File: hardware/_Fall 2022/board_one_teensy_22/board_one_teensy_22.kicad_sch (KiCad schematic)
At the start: 12 parts, among them J1 Conn_01x04, U1 Teensy4.1, U2 BNO055_Breakout, U3 MPL3115A2_Breakout

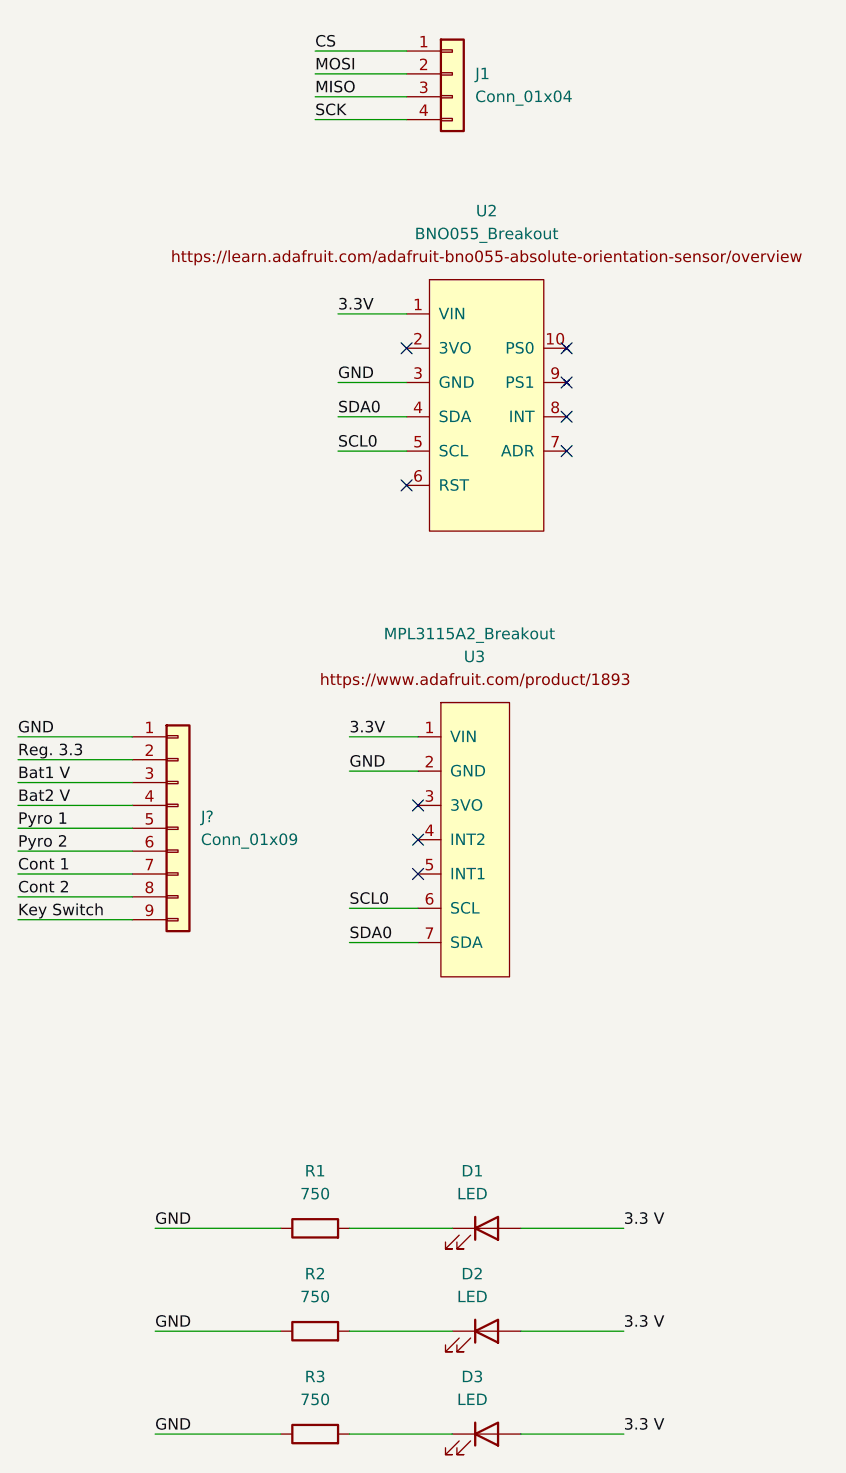
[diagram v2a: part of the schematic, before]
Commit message: Change minor labeling error in teensy boards kicad
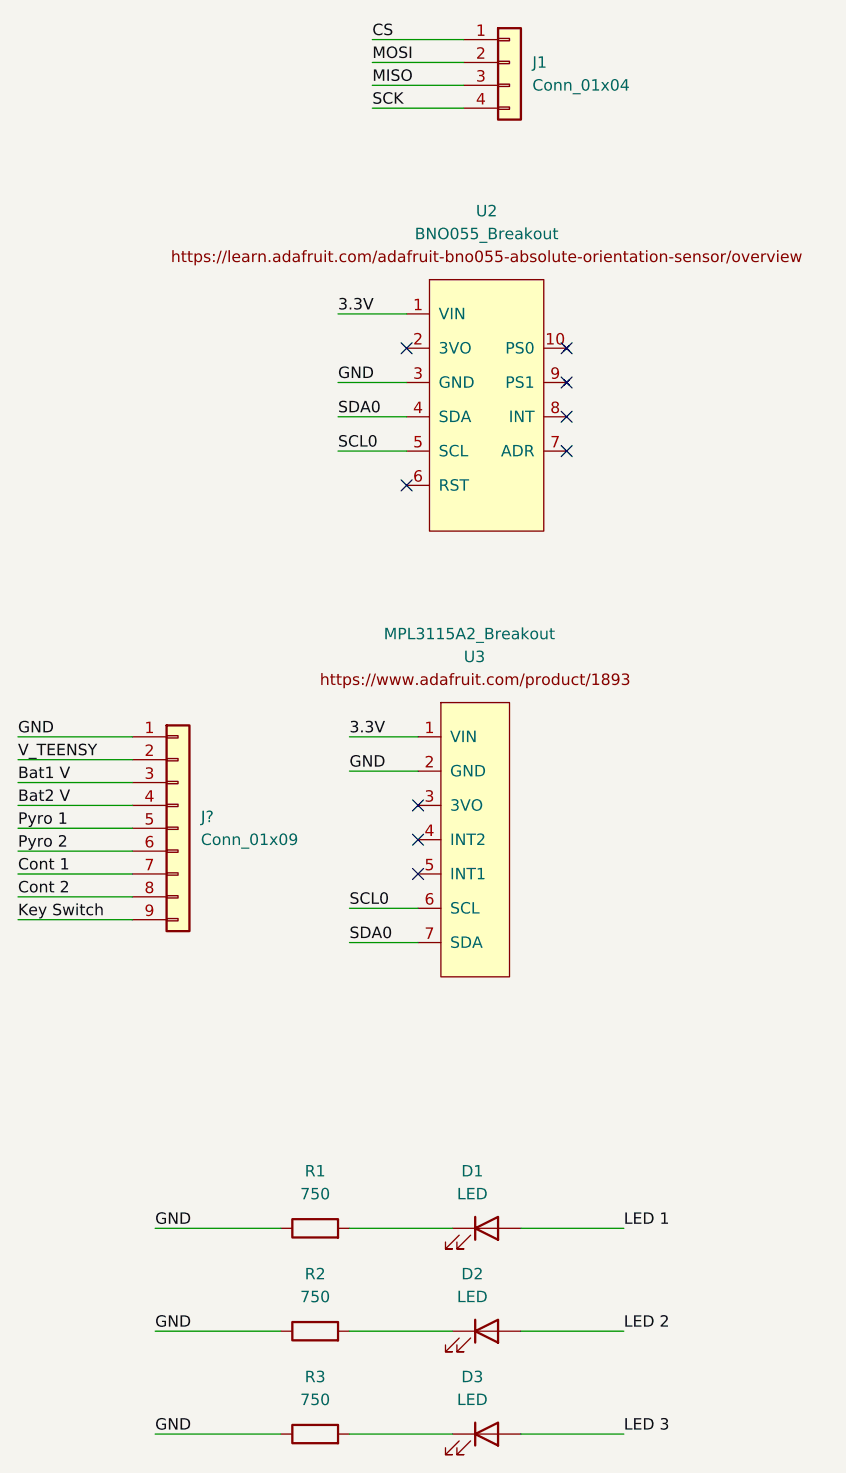
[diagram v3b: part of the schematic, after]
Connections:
- net Reg. 3.3 is gone; now on net V_TEENSY: J?.2 (Pin_2)
- net LED 1: now also D1.2 (A)
- net LED 2: now also D2.2 (A)
- net LED 3: now also D3.2 (A)
- removed net 3.3 V: D1.2 (A), D2.2 (A), D3.2 (A)
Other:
- moved on the sheet: J1
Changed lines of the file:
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@@
   (no_connect (at 95.25 74.93))
   (no_connect (at 231.14 48.26))
-  (wire (pts (xy 85.09 26.67) (xy 95.25 26.67))
+  (wire (pts (xy 91.44 25.4) (xy 101.6 25.4))
     (stroke (width 0) (type default) (color 0 0 0 0))
   )
@@
     (stroke (width 0) (type default) (color 0 0 0 0))
   )
-  (wire (pts (xy 85.09 31.75) (xy 95.25 31.75))
+  (wire (pts (xy 91.44 30.48) (xy 101.6 30.48))
     (stroke (width 0) (type default) (color 0 0 0 0))
   )
@@
     (stroke (width 0) (type default) (color 0 0 0 0))
   )
-  (wire (pts (xy 85.09 29.21) (xy 95.25 29.21))
+  (wire (pts (xy 91.44 27.94) (xy 101.6 27.94))
     (stroke (width 0) (type default) (color 0 0 0 0))
   )
@@
     (stroke (width 0) (type default) (color 0 0 0 0))
   )
-  (wire (pts (xy 85.09 34.29) (xy 95.25 34.29))
+  (wire (pts (xy 91.44 33.02) (xy 101.6 33.02))
     (stroke (width 0) (type default) (color 0 0 0 0))
   )
@@
     (stroke (width 0) (type default) (color 0 0 0 0))
   )
+  (label "LED 1" (at 119.38 157.48 0)
+    (effects (font (size 1.27 1.27)) (justify left bottom))
+  )
   (label "3.3V" (at 87.63 55.88 0)
     (effects (font (size 1.27 1.27)) (justify left bottom))
   )
-  (label "MISO" (at 85.09 31.75 0)
+  (label "MISO" (at 91.44 30.48 0)
     (effects (font (size 1.27 1.27)) (justify left bottom))
   )
@@
     (effects (font (size 1.27 1.27)) (justify left bottom))
   )
+  (label "LED 2" (at 119.38 168.91 0)
+    (effects (font (size 1.27 1.27)) (justify left bottom))
+  )
   (label "Pyro 2" (at 52.07 115.57 0)
     (effects (font (size 1.27 1.27)) (justify left bottom))
@@
     (effects (font (size 1.27 1.27)) (justify left bottom))
   )
-  (label "Reg. 3.3" (at 52.07 105.41 0)
+  (label "V_TEENSY" (at 52.07 105.41 0)
     (effects (font (size 1.27 1.27)) (justify left bottom))
   )
@@
     (effects (font (size 1.27 1.27)) (justify left bottom))
   )
-  (label "3.3 V" (at 119.38 157.48 0)
-    (effects (font (size 1.27 1.27)) (justify left bottom))
-  )
   (label "Key Switch" (at 52.07 123.19 0)
     (effects (font (size 1.27 1.27)) (justify left bottom))
@@
     (effects (font (size 1.27 1.27)) (justify left bottom))
   )
-  (label "3.3 V" (at 119.38 168.91 0)
-    (effects (font (size 1.27 1.27)) (justify left bottom))
-  )
   (label "LED 2" (at 162.56 72.39 0)
     (effects (font (size 1.27 1.27)) (justify left bottom))
@@
     (effects (font (size 1.27 1.27)) (justify left bottom))
   )
-  (label "SCK" (at 85.09 34.29 0)
+  (label "SCK" (at 91.44 33.02 0)
     (effects (font (size 1.27 1.27)) (justify left bottom))
   )
@@
     (effects (font (size 1.27 1.27)) (justify left bottom))
   )
-  (label "3.3 V" (at 119.38 180.34 0)
-    (effects (font (size 1.27 1.27)) (justify left bottom))
-  )
   (label "GND" (at 67.31 157.48 0)
     (effects (font (size 1.27 1.27)) (justify left bottom))
@@
     (effects (font (size 1.27 1.27)) (justify left bottom))
   )
-  (label "CS" (at 85.09 26.67 0)
+  (label "CS" (at 91.44 25.4 0)
     (effects (font (size 1.27 1.27)) (justify left bottom))
   )
@@
     (effects (font (size 1.27 1.27)) (justify left bottom))
   )
-  (label "MOSI" (at 85.09 29.21 0)
+  (label "MOSI" (at 91.44 27.94 0)
+    (effects (font (size 1.27 1.27)) (justify left bottom))
+  )
+  (label "LED 3" (at 119.38 180.34 0)
     (effects (font (size 1.27 1.27)) (justify left bottom))
   )
@@
     (pin "2")
   )
-  (symbol (lib_id "Connector_Generic:Conn_01x04") (at 100.33 29.21 0) (unit 1)
-    (in_bom yes) (on_board yes) (fields_autoplaced)
-    (property "Reference" "J1" (id 0) (at 102.87 29.2099 0)
+  (symbol (lib_id "Connector_Generic:Conn_01x04") (at 106.68 27.94 0) (unit 1)
+    (in_bom yes) (on_board yes) (fields_autoplaced)
+    (property "Reference" "J1" (id 0) (at 109.22 27.9399 0)
       (effects (font (size 1.27 1.27)) (justify left))
     )
-    (property "Value" "Conn_01x04" (id 1) (at 102.87 31.7499 0)
+    (property "Value" "Conn_01x04" (id 1) (at 109.22 30.4799 0)
       (effects (font (size 1.27 1.27)) (justify left))
     )
-    (property "Footprint" "" (id 2) (at 100.33 29.21 0)
-      (effects (font (size 1.27 1.27)) hide)
-    )
-    (property "Datasheet" "~" (id 3) (at 100.33 29.21 0)
-      (effects (font (size 1.27 1.27)) hide)
-    )
+    (property "Footprint" "" (id 2) (at 106.68 27.94 0)
+      (effects (font (size 1.27 1.27)) hide)
+    )
+    (property "Datasheet" "~" (id 3) (at 106.68 27.94 0)
+      (effects (font (size 1.27 1.27)) hide)
+    )

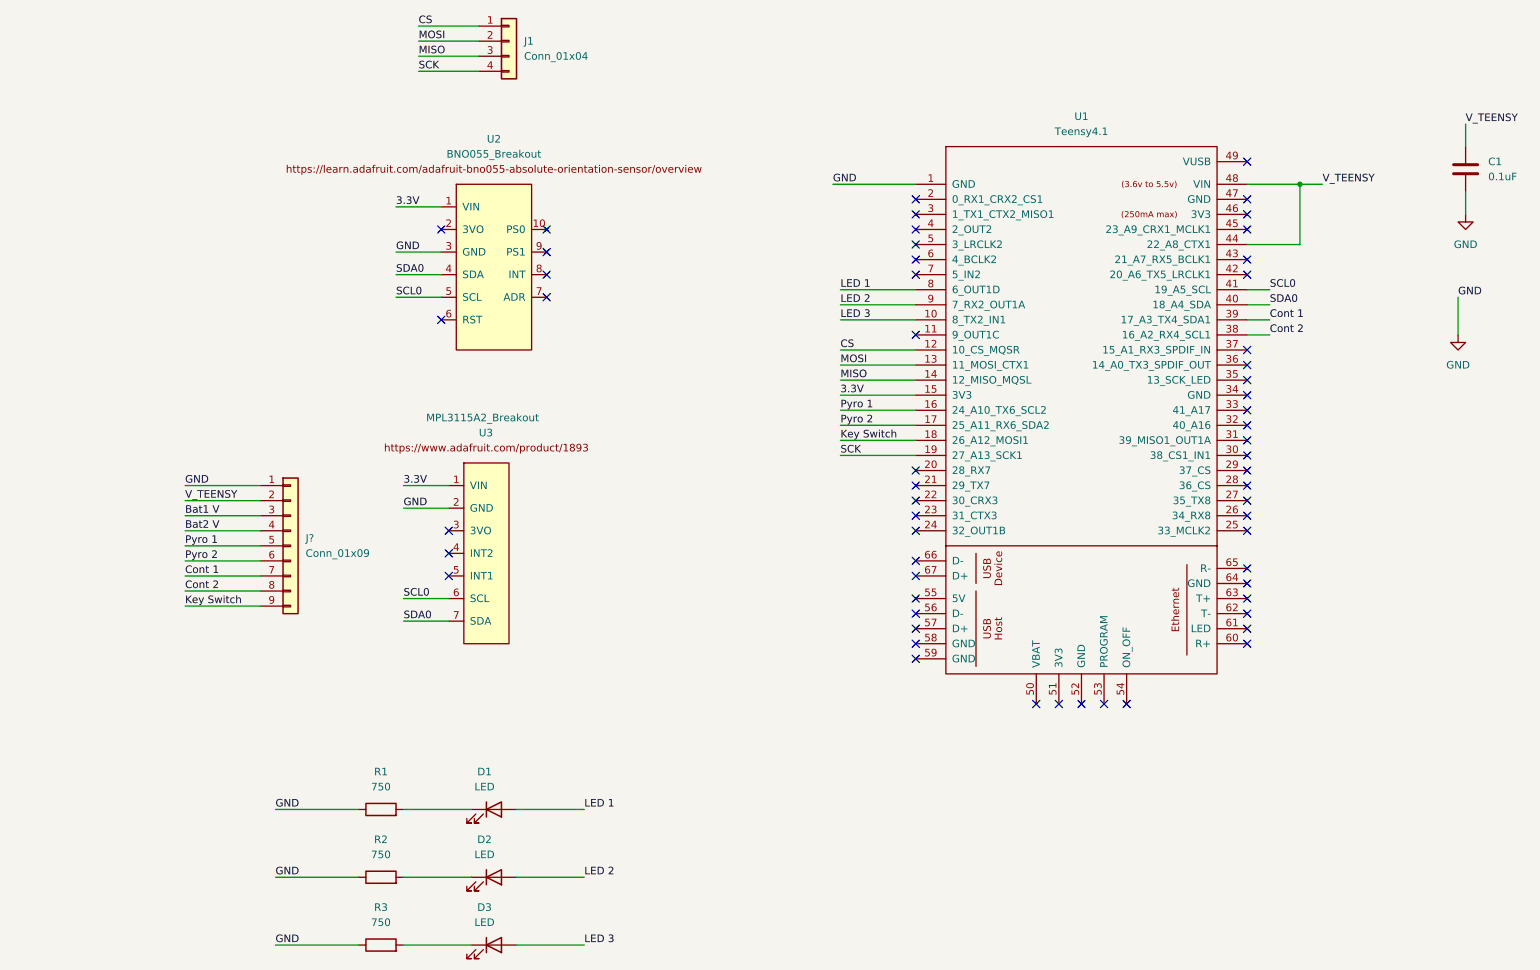
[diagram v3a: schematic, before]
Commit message: Update now teensy connection
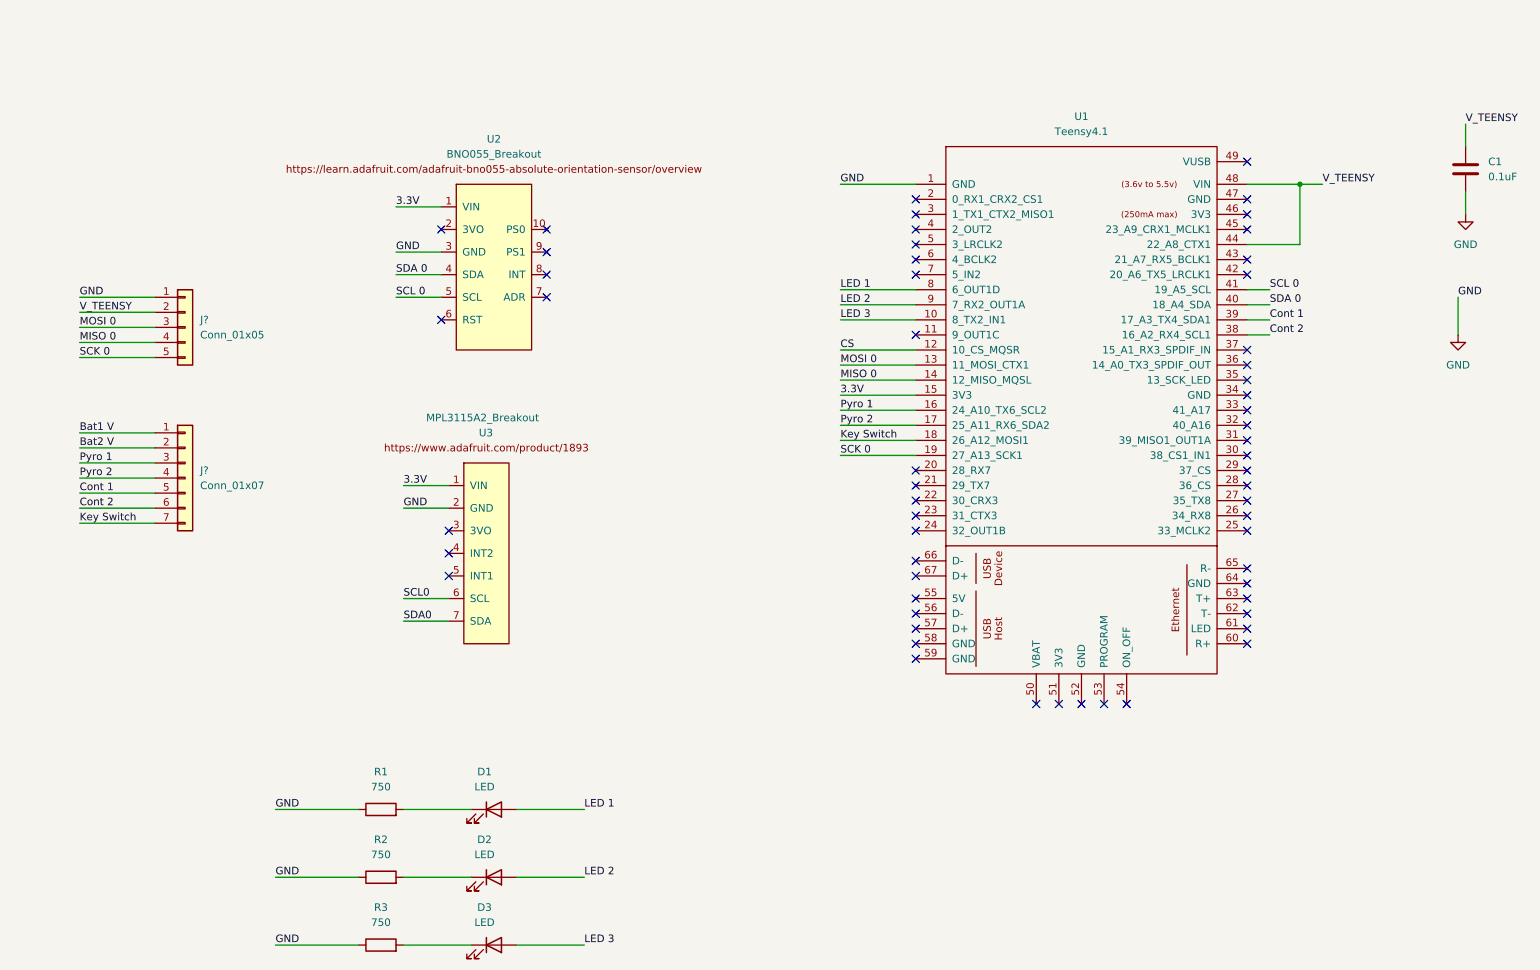
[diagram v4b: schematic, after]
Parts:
- removed J1: Conn_01x04, symbol Connector_Generic:Conn_01x04
- removed J?: Conn_01x09, symbol Connector_Generic:Conn_01x09
- added J?: Conn_01x05, symbol Connector_Generic:Conn_01x05
- added J?: Conn_01x07, symbol Connector_Generic:Conn_01x07
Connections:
- net Bat1 V: now also J?.1 (Pin_1)
- net Bat2 V: now also J?.2 (Pin_2)
- net Cont 1: now also J?.5 (Pin_5)
- net Cont 2: now also J?.6 (Pin_6)
- net GND: now also J?.1 (Pin_1)
- net Key Switch: now also J?.7 (Pin_7)
- net Pyro 1: now also J?.3 (Pin_3)
- net Pyro 2: now also J?.4 (Pin_4)
- net SCL0: no longer U1.41 (19_A5_SCL), U2.5 (SCL)
- net SDA0: no longer U1.40 (18_A4_SDA), U2.4 (SDA)
- net V_TEENSY: now also J?.2 (Pin_2)
- net MISO renamed MISO 0
- net MISO 0: now also J?.4 (Pin_4)
- net MOSI renamed MOSI 0
- net MOSI 0: now also J?.3 (Pin_3)
- net SCK renamed SCK 0
- net SCK 0: now also J?.5 (Pin_5)
- new net SCL 0: U1.41 (19_A5_SCL), U2.5 (SCL)
- new net SDA 0: U1.40 (18_A4_SDA), U2.4 (SDA)
